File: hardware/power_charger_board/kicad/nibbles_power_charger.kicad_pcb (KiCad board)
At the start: 4 copper layers, 148 x 70 mm, 95 parts, among them J12 JST-GH 6 (charger port: I2C), J2 XT30PW-M (dock power, from th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, J23 JST-GH 6 (to the power board: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, J3 XT30 (pack, from 4S BMS), J4 NTC 103AT on the cells, J5 XT30 (to the 5 V lighting con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, J6 To the base board (JST-GH 8), J7 S3B-PH-K-S (dock data, from t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, J8 S2B-PH-K-S (dock LED, panel), J9 JST-GH 6 (keypad port: I2C), Q5 30V N-FET >= 15 A, Q6 30V N-FET >= 15 A, Q7 2N7002, Q8 2N7002, Q9 30V N-FET >= 15 A, U2 BQ25798RQMR, U3 LM74700-Q1 (dock), U4 LM74700-Q1 (pack), U5 TPS259827ONRGET, U6 INA226AIDGSR, U7 TPS62933DRLR, U8 TCA9534PWR, U9 LM74700-Q1 (LEMO)

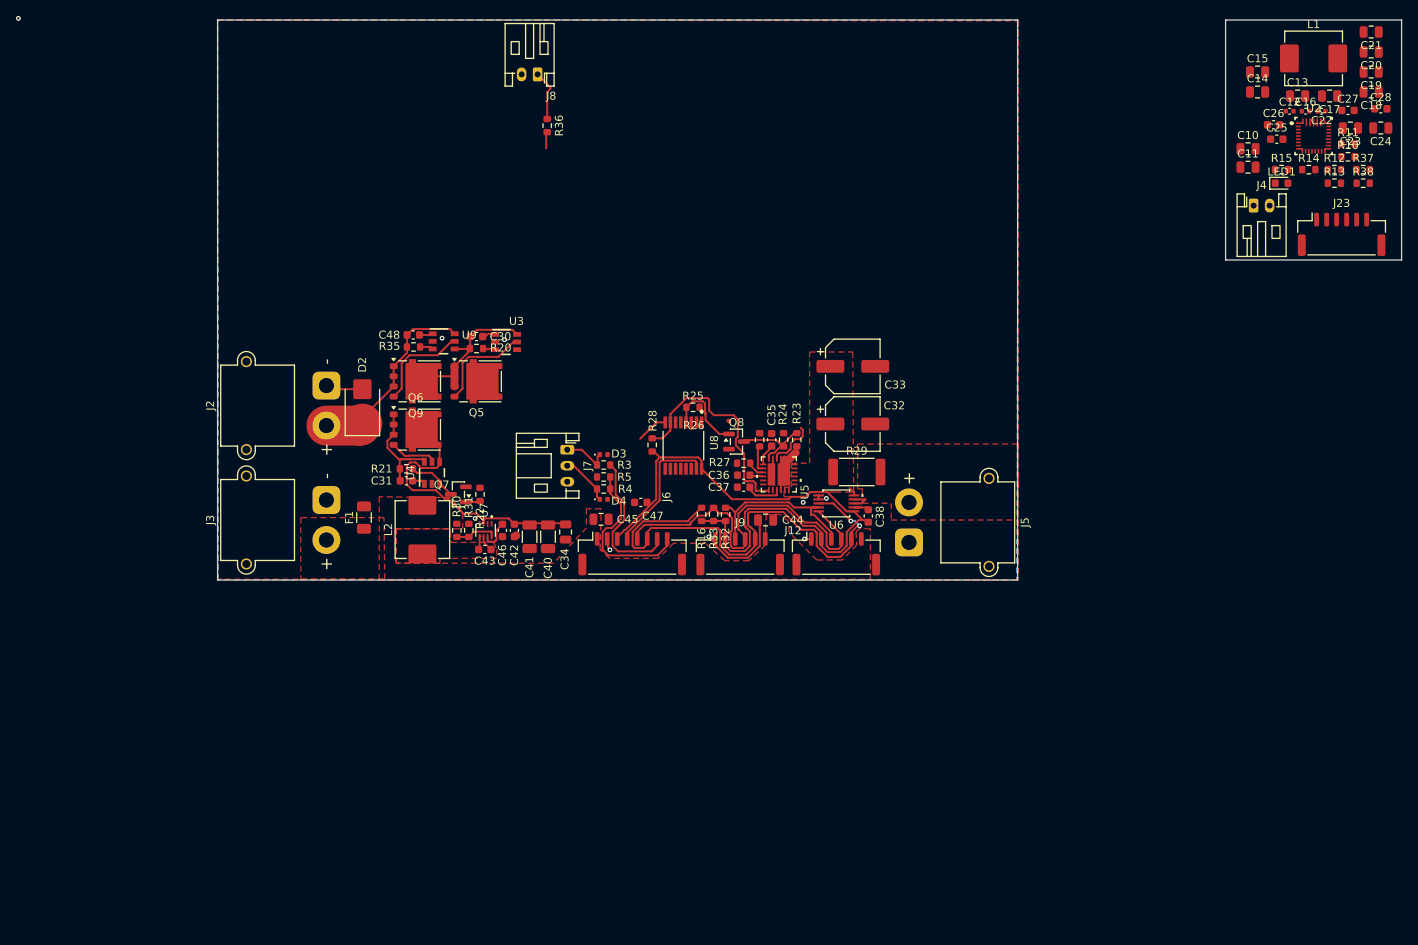
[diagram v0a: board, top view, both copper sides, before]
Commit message: Power + charger board: KXUSBC2 charger layout, test points, J6 fix, layout routed
- Charger section copied from KXUSBC2's BQ25792 layout (placement, tracks,
  vias, zones), KX-only parts dropped; R10-R13/C28 to 0402; dock input
  snubber R39/C49/C50; minimums relaxed to JLCPCB/KX values
- J6 footprint corrected (board top faces the 3.49's battery side, screen
  up), its holes on User.Drawings, 3D model 11 mm up; D5 to A11 and
  DOCK_DET to A6, R3 to B6
- Connectors all vertical JST-GH; J12/J23 removed; J10 (GH8 cable to the
  3.49) and J11 (second I2C port) added; H1-H3 M2.5 holes; connector
  labels and board name
- Test points TP3-TP24 on the bottom; CHG_ILIM and EFUSE_IMON named
- Schematic: DOCK_DATA_RAW/DOCK_DET_RAW short removed, C30 pins matched
- Routing by hand in KiCad (in progress; review findings still open)

Co-Authored-By: Claude Opus 5.5 <noreply@anthropic.com>
Claude-Session: https://claude.ai/code/session_01UUhpevE9ZSCJvyu3edQmf9
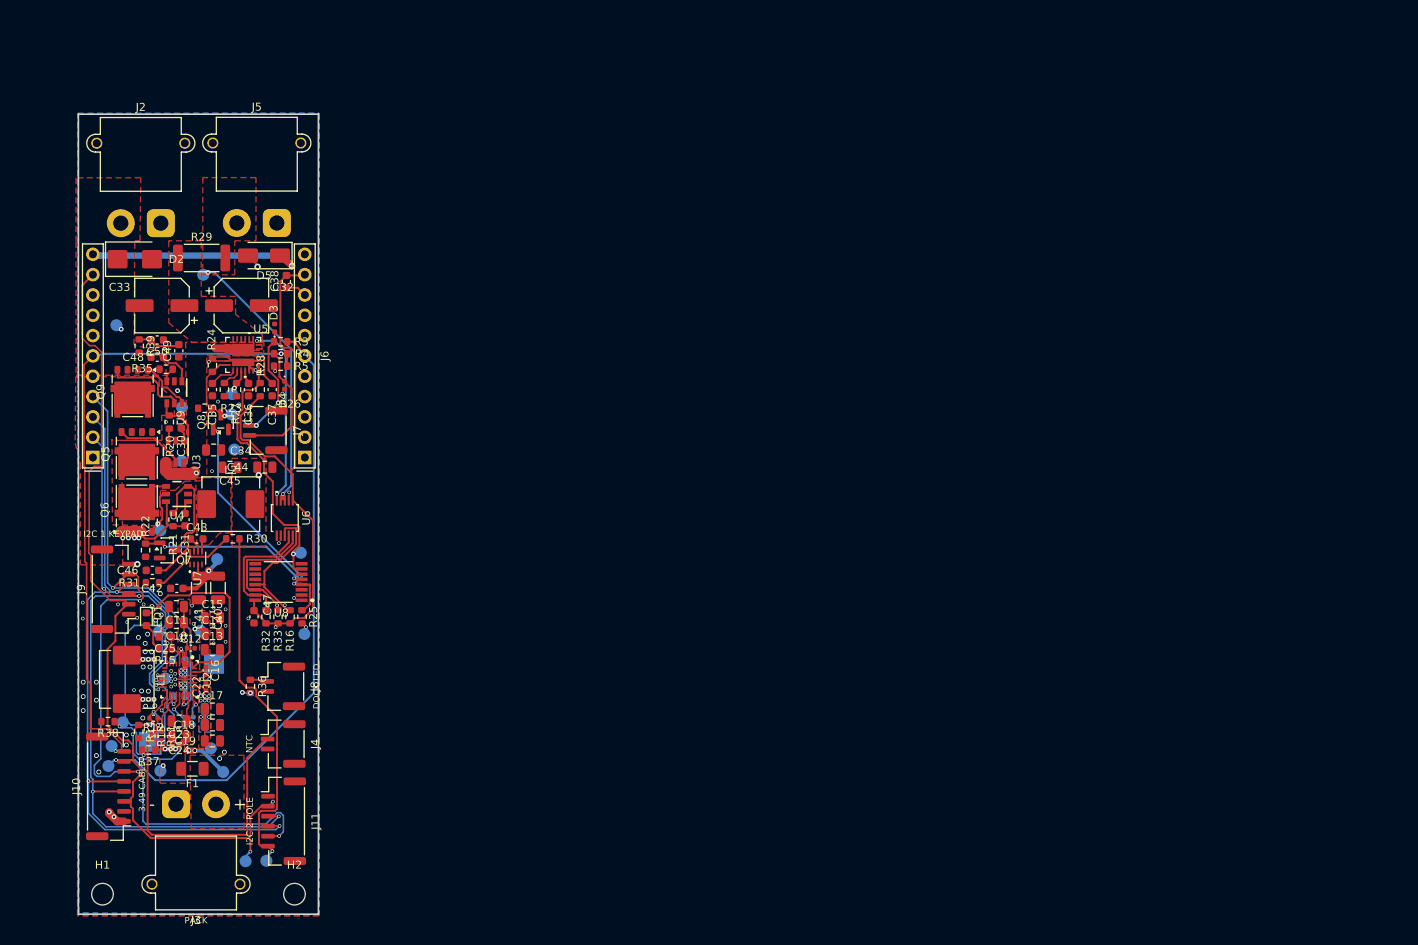
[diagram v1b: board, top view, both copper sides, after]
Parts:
- removed J12: JST-GH 6 (charger port: I2C), Connector_JST:JST_GH_SM06B-GHS-TB_1x06-1MP_P1.25mm_Horizontal
- removed J23: JST-GH 6 (to the power board: I2C), Connector_JST:JST_GH_SM06B-GHS-TB_1x06-1MP_P1.25mm_Horizontal
- added C49: 1uF 50V, Capacitor_SMD:C_0603_1608Metric, F.Cu at (45.1, 91.3)
- added C50: 1uF 50V, Capacitor_SMD:C_0603_1608Metric, F.Cu at (42.5, 90.0)
- added D5: SS34, Diode_SMD:D_SMA, F.Cu at (55.8, 79.5)
- added H1: M2.5, MountingHole:MountingHole_2.7mm_M2.5, F.Cu at (35.6, 159.3)
- added H2: M2.5, MountingHole:MountingHole_2.7mm_M2.5, F.Cu at (59.6, 159.3)
- added J10: JST-GH 8 vertical (cable to the 3.49, instead of J6), Connector_JST:JST_GH_BM08B-GHS-TBT_1x08-1MP_P1.25mm_Vertical, F.Cu at (36.4, 145.8)
- added J11: JST-GH 6 vertical (I2C port 2: pole segment), Connector_JST:JST_GH_BM06B-GHS-TBT_1x06-1MP_P1.25mm_Vertical, F.Cu at (58.2, 150.2)
- added R39: 2 (input snubber), Resistor_SMD:R_0603_1608Metric, F.Cu at (40.2, 90.8)
- added TP1: GND, TestPoint:TestPoint_Pad_2.5x2.5mm, B.Cu at (49.5, 130.5)
- added TP10: +5V, TestPoint:TestPoint_Pad_D1.5mm, B.Cu at (56.1, 155.1)
- added TP11: +3V3, TestPoint:TestPoint_Pad_D1.5mm, B.Cu at (53.5, 155.2)
- added TP12: SYS, TestPoint:TestPoint_Pad_D1.5mm, B.Cu at (49.1, 141.0)
- added TP13: PMID, TestPoint:TestPoint_Pad_D1.5mm, B.Cu at (47.9, 126.3)
- added TP14: REGN, TestPoint:TestPoint_Pad_D1.5mm, B.Cu at (42.6, 126.5)
- added TP15: EFUSE_IMON, TestPoint:TestPoint_Pad_D1.5mm, B.Cu at (51.8, 96.8)
- added TP16: CHG_ILIM, TestPoint:TestPoint_Pad_D1.5mm, B.Cu at (38.1, 137.8)
- added TP17: EFUSE_PG, TestPoint:TestPoint_Pad_D1.5mm, B.Cu at (60.4, 116.6)
- added TP18: EFUSE_EN, TestPoint:TestPoint_Pad_D1.5mm, B.Cu at (51.8, 99.3)
- added TP19: GATE_DOCK, TestPoint:TestPoint_Pad_D1.5mm, B.Cu at (45.5, 105.2)
- added TP2: TS, TestPoint:TestPoint_Pad_2.5x2.5mm, B.Cu at (41.4, 140.2)
- added TP20: GATE_PACK, TestPoint:TestPoint_Pad_D1.5mm, B.Cu at (42.9, 113.8)
- added TP21: GATE_LEMO, TestPoint:TestPoint_Pad_D1.5mm, B.Cu at (45.5, 98.4)
- added TP22: CHG_QON, TestPoint:TestPoint_Pad_D1.5mm, B.Cu at (43.5, 132.3)
- added TP23: DOCK_DET, TestPoint:TestPoint_Pad_D1.5mm, B.Cu at (36.8, 140.8)
- added TP24: DOCK_UART, TestPoint:TestPoint_Pad_D1.5mm, B.Cu at (36.4, 143.2)
- added TP3: GND, TestPoint:TestPoint_Pad_D1.5mm, B.Cu at (60.9, 126.8)
- added TP4: GND, TestPoint:TestPoint_Pad_D1.5mm, B.Cu at (52.1, 103.7)
- added TP5: DOCK_RAW, TestPoint:TestPoint_Pad_D1.5mm, B.Cu at (37.4, 88.2)
- added TP6: DOCK_VIN, TestPoint:TestPoint_Pad_D1.5mm, B.Cu at (50.7, 144.0)
- added TP7: PACK_F, TestPoint:TestPoint_Pad_D1.5mm, B.Cu at (42.9, 143.8)
- added TP8: LIGHT_BUS, TestPoint:TestPoint_Pad_D1.5mm, B.Cu at (50.0, 117.4)
- added TP9: LIGHT_OUT, TestPoint:TestPoint_Pad_D1.5mm, B.Cu at (48.2, 81.8)
- C20, C21, C26, C27: moved to B.Cu
- C28: footprint Capacitor_SMD:C_0603_1608Metric -> Capacitor_SMD:C_0402_1005Metric; moved to B.Cu
- J4: value NTC 103AT on the cells -> NTC 103AT on the cells (JST-GH 2, vertical); footprint Connector_JST:JST_PH_S2B-PH-K_1x02_P2.00mm_Horizontal -> Connector_JST:JST_GH_BM02B-GHS-TBT_1x02-1MP_P1.25mm_Vertical
- J6: value To the base board (JST-GH 8) -> To the 3.49 (stacked headers); footprint Connector_JST:JST_GH_SM08B-GHS-TB_1x08-1MP_P1.25mm_Horizontal -> nibbles:Waveshare_ESP32-S3-Touch-LCD-3.49_Headers
- J7: value S3B-PH-K-S (dock data, from the LEMO) -> BM02B-GHS-TBT (dock data + detect, from the LEMO); footprint Connector_JST:JST_PH_S3B-PH-K_1x03_P2.00mm_Horizontal -> Connector_JST:JST_GH_BM02B-GHS-TBT_1x02-1MP_P1.25mm_Vertical
- J8: value S2B-PH-K-S (dock LED, panel) -> BM02B-GHS-TBT (dock LED, panel); footprint Connector_JST:JST_PH_S2B-PH-K_1x02_P2.00mm_Horizontal -> Connector_JST:JST_GH_BM02B-GHS-TBT_1x02-1MP_P1.25mm_Vertical
- J9: value JST-GH 6 (keypad port: I2C) -> JST-GH 6 vertical (keypad port: I2C); footprint Connector_JST:JST_GH_SM06B-GHS-TB_1x06-1MP_P1.25mm_Horizontal -> Connector_JST:JST_GH_BM06B-GHS-TBT_1x06-1MP_P1.25mm_Vertical
- R10: footprint Resistor_SMD:R_0603_1608Metric -> Resistor_SMD:R_0402_1005Metric; moved to B.Cu
- R11, R12, R13: footprint Resistor_SMD:R_0603_1608Metric -> Resistor_SMD:R_0402_1005Metric
- moved R38 170.7 mm to (36.3, 137.7), turned to 180 degrees
- moved C21 168.8 mm to (49.4, 138.1), turned to 0 degrees
- moved C24 168.4 mm to (45.2, 139.6)
- moved R37 168.2 mm to (41.4, 141.2), turned to 180 degrees
- moved L1 167.4 mm to (38.6, 132.4), turned to -90 degrees
- moved C19 167.3 mm to (49.4, 140.1), turned to 0 degrees
- moved C28 167.0 mm to (47.0, 137.6), turned to -90 degrees
- moved C20 166.5 mm to (49.4, 136.1), turned to 0 degrees
- moved R11 165.7 mm to (43.0, 139.5), turned to -90 degrees
- moved C18 165.0 mm to (49.4, 138.1), turned to 0 degrees
- moved C23 164.1 mm to (45.2, 137.6)
- moved C27 163.5 mm to (45.1, 134.5)
- moved R13 163.2 mm to (41.8, 139.5), turned to -90 degrees
- moved R12 162.8 mm to (42.0, 137.3), turned to 180 degrees
- moved R14 162.2 mm to (40.1, 138.9), turned to -90 degrees
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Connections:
- net Net-(U2-ILIM_HIZ) renamed CHG_ILIM
- net Net-(U2-TS) renamed CHG_TS
- net Net-(U5-IMON) renamed EFUSE_IMON
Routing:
- net +3V3: track 79.4 -> 197.9 mm, vias 0 -> 3
- net PWR_SDA: track 39.0 -> 147.2 mm, vias 0 -> 6
- net PWR_SCL: track 47.3 -> 150.2 mm, vias 0 -> 5
- net PWR_INT: track 62.8 -> 165.3 mm, vias 2 -> 6
- net +5V_349: track 0.00 -> 102.2 mm, vias 0 -> 3
- net +5V: track 0.00 -> 99.6 mm, vias 0 -> 4
- net DOCK_DET: track 20.7 -> 80.9 mm, vias 0 -> 2
- net DOCK_UART: track 18.4 -> 78.3 mm, vias 0 -> 1
- net PACK_F: track 14.2 -> 71.5 mm, vias 0 -> 8
- net CHG_TS: track 0.00 -> 49.4 mm, vias 0 -> 1
- net LIGHT_OUT: track 3.28 -> 35.4 mm, vias 0 -> 2
- net REGN: track 0.00 -> 30.2 mm, vias 0 -> 2
- net DOCK_VIN: track 21.9 -> 50.8 mm, vias 0 -> 9
- net Net-(LED1-C): track 0.00 -> 24.0 mm
- net EFUSE_OUT: track 1.16 -> 23.2 mm, vias 0 -> 2
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- added copper zone on F.Cu, net DOCK_RAW
- added copper zone on F.Cu, net DOCK_VIN
- added copper zone on In2.Cu, net DOCK_VIN
- added copper zone on In2.Cu, net GND
- added copper zone on F.Cu, net LIGHT_BUS
- added copper zone on F.Cu, net PACK_F
- added copper zone on F.Cu, net PMID
- added copper zone on B.Cu, net SW1
- added copper zone on F.Cu, net SW1
- added copper zone on In2.Cu, net SW1
- added copper zone on B.Cu, net SW2
- added copper zone on F.Cu, net SW2
- added copper zone on In2.Cu, net SW2
- added copper zone on B.Cu, net SYS
- added copper zone on F.Cu, net SYS
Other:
- board size 148 x 70 mm -> 30 x 100 mm
- board text added: "NIBBLES POWER + CHARGER rev A 2026-10"

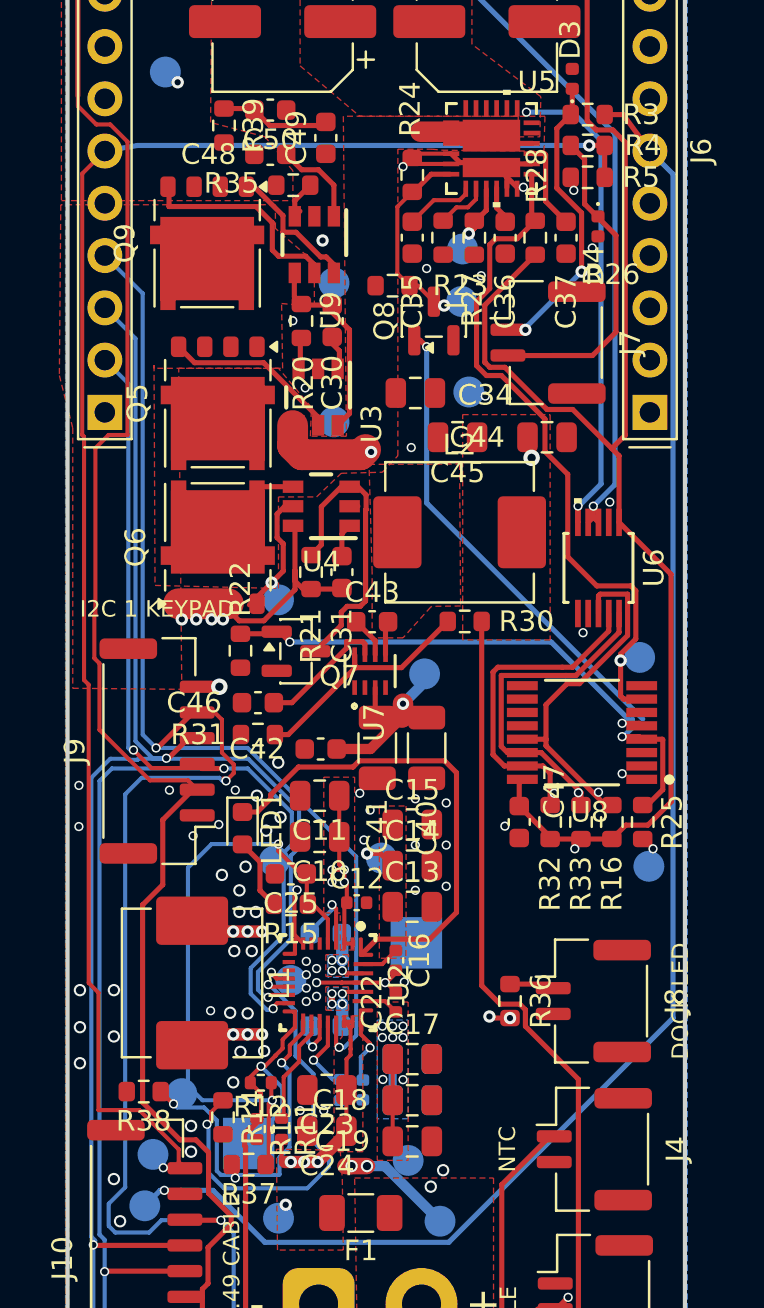
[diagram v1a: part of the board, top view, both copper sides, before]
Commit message: Power + charger board: review fixes and more routing
- Mechanical fixes from the layout review: Solid zone connections on the
  pack XT30, F1 and the eFuse input pins and on starved ground pads;
  ground vias for floating ground pads; test pads moved off other nets
  and wired; ground vias nudged clear; dangling stubs removed
- Further routing by hand in KiCad

Co-Authored-By: Claude Opus 5.5 <noreply@anthropic.com>
Claude-Session: https://claude.ai/code/session_01UUhpevE9ZSCJvyu3edQmf9
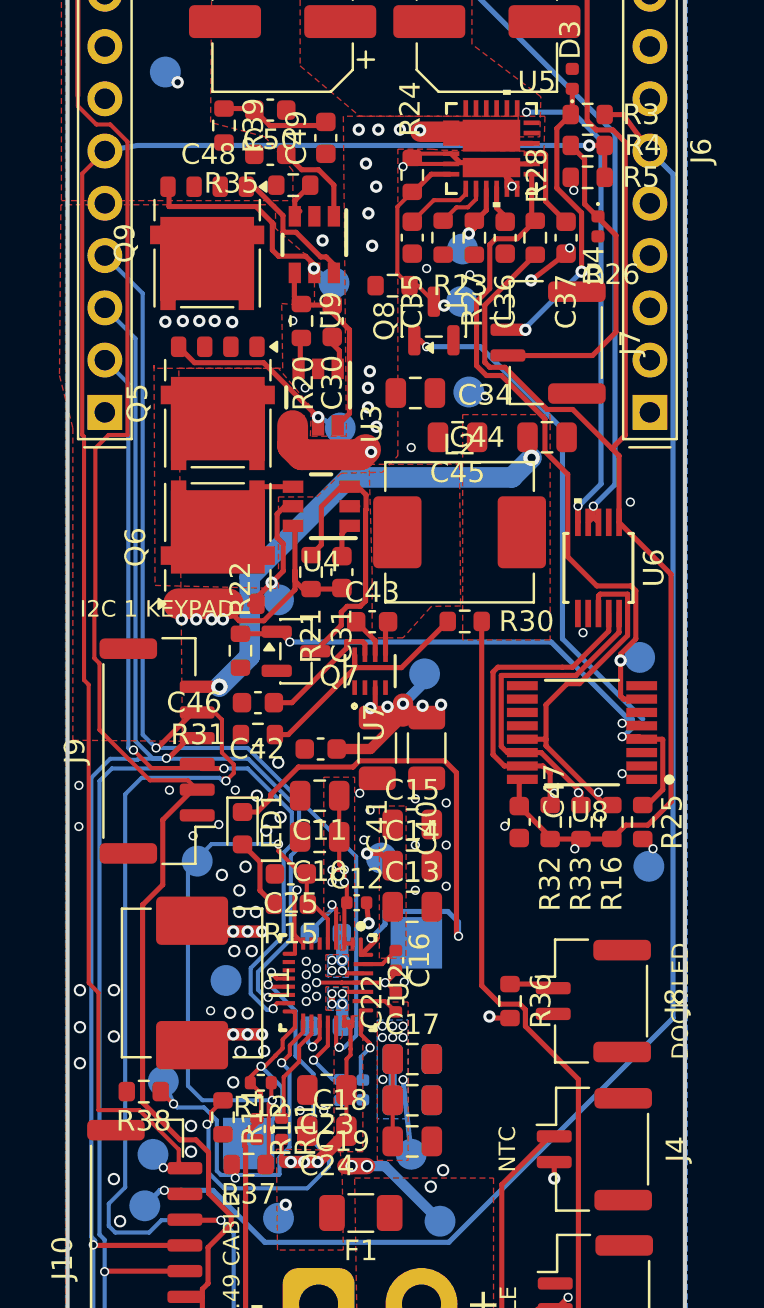
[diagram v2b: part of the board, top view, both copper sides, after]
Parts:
- moved TP14 3.75 mm to (38.9, 126.5)
- moved TP22 3.15 mm to (40.3, 132.3)
- moved TP16 1.08 mm to (37.2, 137.2)
- moved TP19 0.42 mm to (45.9, 105.5)
- moved TP12 0.34 mm to (49.3, 140.7)
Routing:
- net GND: track 21.9 -> 25.8 mm, vias 70 -> 73
- net SYS: track 8.12 -> 11.8 mm
- net Net-(LED1-C): track 24.0 -> 26.9 mm, vias 0 -> 2
- net +5V: track 99.6 -> 97.9 mm
- net LIGHT_OFF: track 30.0 -> 31.5 mm
- net CHG_ILIM: track 18.0 -> 19.2 mm
- net GATE_LEMO: track 10.4 -> 11.6 mm, vias 0 -> 1
- net GATE_DOCK: track 9.00 -> 10.2 mm, vias 0 -> 1
- net +5V_349: track 102.2 -> 103.2 mm
- net PWR_SDA: track 147.2 -> 146.5 mm
- net LIGHT_BUS: track 42.1 -> 41.9 mm, vias 2 -> 18
- net DOCK_VIN: vias 9 -> 13
- added copper zone on In2.Cu, net LIGHT_BUS
- added copper zone on In2.Cu, net PACK_F

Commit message: Power + charger board: routing finished, DRC clean (silkscreen aside)
- Ground vias, PACK_F pours and vias, LIGHT_BUS and DOCK_VIN pours on In2,
  charger feed, test points wired (by hand in KiCad)
- Review fixes: vias slid off other nets' copper, PACK_F vias on the CE
  track replaced with clear ones, stray stitching vias dropped, +5V into
  D5 widened to 0.8 mm, STAT track clear of C11
- ERC clean, schematic parity 0, DRC 0 errors besides silkscreen, 0 unrouted

Co-Authored-By: Claude Opus 5.5 <noreply@anthropic.com>
Claude-Session: https://claude.ai/code/session_01UUhpevE9ZSCJvyu3edQmf9
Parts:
- moved TP22 0.30 mm to (40.0, 132.3)
- moved R15 0.25 mm to (43.7, 128.6)
- moved R23 0.09 mm to (48.3, 98.5)
- moved C10 0.05 mm to (44.8, 125.3)
- moved C11 0.05 mm to (44.8, 123.3)
- moved C41 0.05 mm to (47.7, 121.0)
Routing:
- net CHG_QON: track 1.00 -> 4.24 mm
- net DOCK_VIN: track 50.8 -> 53.9 mm
- net GND: track 25.8 -> 28.8 mm, vias 73 -> 85
- net CHG_TS: track 49.4 -> 50.9 mm
- net LIGHT_OFF: track 31.5 -> 32.1 mm
- net PACK_F: track 71.5 -> 71.4 mm, vias 8 -> 20
